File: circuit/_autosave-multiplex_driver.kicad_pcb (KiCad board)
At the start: 2 copper layers, 46 parts, among them P1 Keypad, P2 I2C, P3 +5V, P4 Anodes, P5 Cathode 1-8, P6 Cathode 9-16, P7 Serial, P8 +24V, Q1 BC546A, Q2 BC546A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

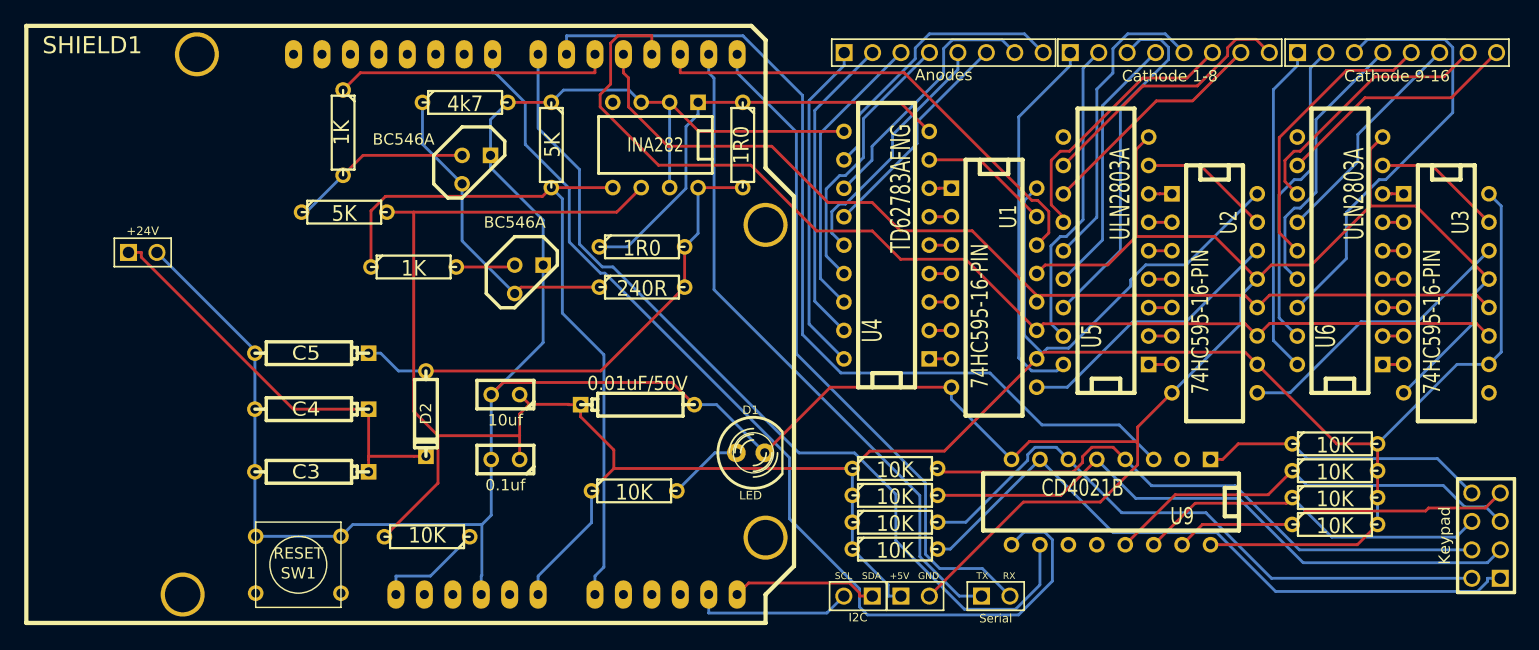
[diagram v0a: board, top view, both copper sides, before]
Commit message: Added input for keypad
the uno model includes the ability to connect to a keypad.
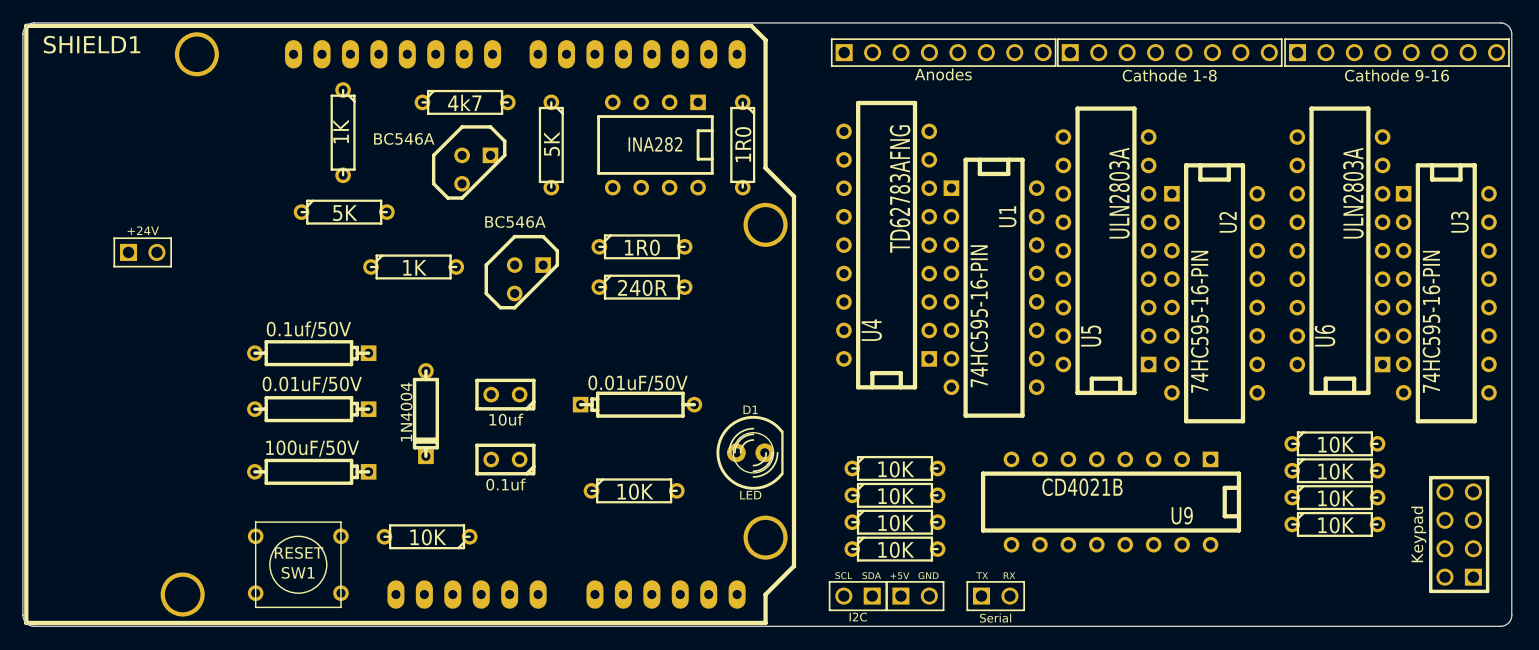
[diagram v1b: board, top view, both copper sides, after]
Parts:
- moved P1 2.40 mm to (140.3, 58.6)
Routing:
- net GND: track 327.8 -> 0.00 mm
- net +5V: track 278.6 -> 0.00 mm
- net M-SRCLK: track 101.0 -> 0.00 mm
- net M-RCLK: track 90.7 -> 0.00 mm
- net K-RCLK: track 90.2 -> 0.00 mm
- net K-SER: track 82.3 -> 0.00 mm
- net K-SRCLK: track 80.1 -> 0.00 mm
- net M-SENSE: track 66.1 -> 0.00 mm
- net N-0000012: track 60.7 -> 0.00 mm
- net N-0000013: track 59.7 -> 0.00 mm
- net N-0000060: track 59.1 -> 0.00 mm
- net N-0000079: track 55.9 -> 0.00 mm
- net N-0000062: track 55.6 -> 0.00 mm
- net N-0000078: track 52.9 -> 0.00 mm
- net N-00000100: track 45.4 -> 0.00 mm
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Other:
- board outline added: 133 x 53.9 mm
